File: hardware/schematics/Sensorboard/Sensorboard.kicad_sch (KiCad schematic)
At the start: 79 parts, among them J1 Grauwasser, J2 Switch/Solder Jumper, J3 BME680 #0 Innen, J5 BME280 #1 Außen, J6 HX711 GasWaage, J7 LT452 Malibu, J8 Frischwasser, J9 USB Power, Q1 IRLML2244, Q2 IRLML2244, Q3 IRLML2244, Q4 AO3401A, Q5 2N7002, Q6 IRLML2244, Q7 IRLML2244, U1 ESP32-S3-DevKitC, U2 TSR2-2450, U3 LDL1117S33R, U5 PCF8523T, U6 BNO055, U7 INA226, Y1 32.768, Y2 32.768

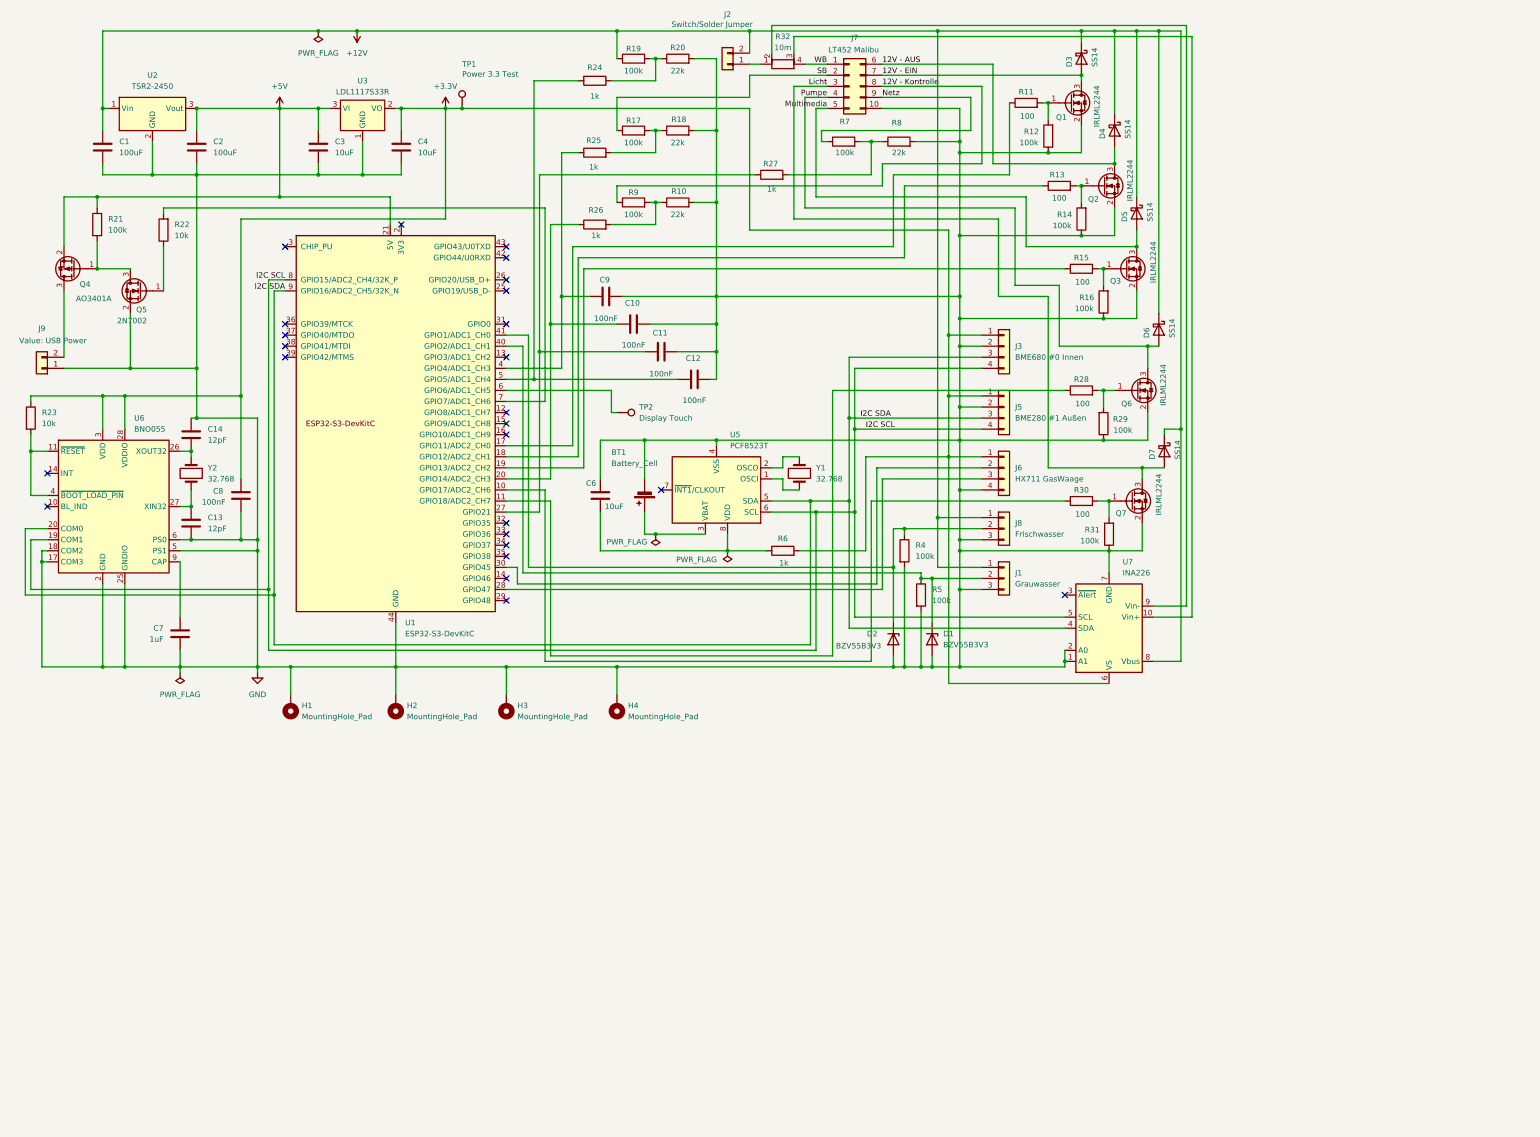
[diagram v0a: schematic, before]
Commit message: chore: OpenWiki, Sensorboard-/ruuvitag_gas-Schaltplaene, Log-Level und Doku nachgezogen
- OpenWiki-Index (openwiki/, AGENTS.md) und Verweis in CLAUDE.md
- Sensorboard-Schaltplan/PCB und ruuvitag_gas-Schaltplan aktualisiert
- LDL1117S33R-Bauteilbibliothek, Material-Icon-Font 16 px
- display_config.h: Log-Level Main/Theme auf WARN, Screenshot-Block aufgeraeumt
- gasbee_nrf/README: HX711-Modul und AVDD-Spannungsteiler beschrieben
- ruuvitag_hw (Fremd-Repo) in .gitignore

Co-Authored-By: Claude Opus 5.5 <noreply@anthropic.com>
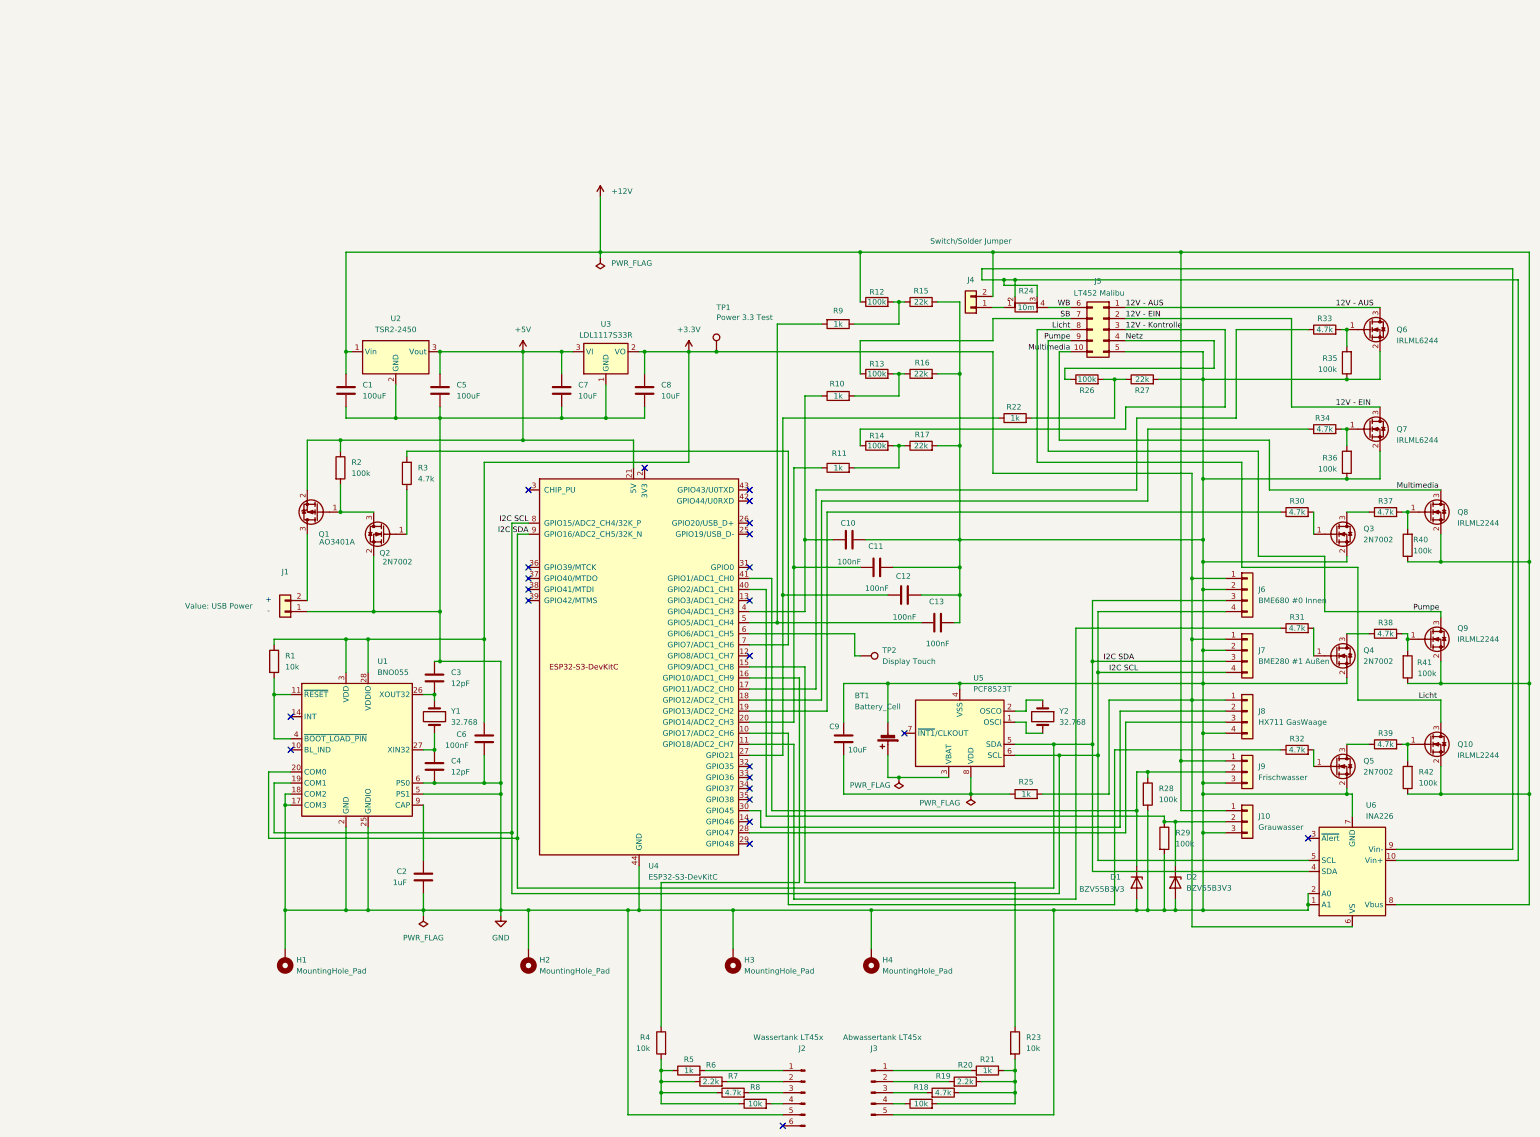
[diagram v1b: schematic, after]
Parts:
- removed D3, D4, D5, D6, D7: SS14, Diode_SMD:D_SMA, symbol Diode:SS14
- removed Q1, Q2: IRLML2244, Package_TO_SOT_SMD:SOT-23, symbol Transistor_FET:BSS138
- added J2: Wassertank LT45x, Connector_Molex:Molex_Micro-Fit_3.0_43650-0615_1x06_P3.00mm_Vertical, symbol Connector:Conn_01x06_Pin
- added J3: Abwassertank LT45x, Connector_Molex:Molex_Micro-Fit_3.0_43650-0515_1x05_P3.00mm_Vertical, symbol Connector:Conn_01x05_Pin
- added Q3, Q4, Q5: 2N7002, Package_TO_SOT_SMD:SOT-23, symbol Transistor_FET:2N7002
- added Q6, Q7: IRLML6244, Package_TO_SOT_SMD:SOT-23, symbol Transistor_FET:IRLML6244
- added R18, R23, R4, R8: 10k, Resistor_SMD:R_0402_1005Metric, symbol Device:R
- added R19, R30, R31, R32, R7: 4.7k, Resistor_SMD:R_0402_1005Metric, symbol Device:R
- added R20, R6: 2.2k, Resistor_SMD:R_0402_1005Metric, symbol Device:R
- added R21, R5: 1k, Resistor_SMD:R_0402_1005Metric, symbol Device:R
- R3: renamed from R22; value 10k -> 4.7k
- R33: renamed from R11; value 100 -> 4.7k
- R34: renamed from R13; value 100 -> 4.7k
- R37: renamed from R15; value 100 -> 4.7k
- R38: renamed from R28; value 100 -> 4.7k
- R39: renamed from R30; value 100 -> 4.7k
- renumbered C9 to C10, C10 to C11, C11 to C12, C12 to C13, C7 to C2, C14 to C3, C13 to C4, C2 to C5, C8 to C6, C3 to C7, C4 to C8, C6 to C9, D2 to D1, D1 to D2, J9 to J1, J1 to J10, J2 to J4, J7 to J5, J3 to J6, J5 to J7, J6 to J8, J8 to J9, Q4 to Q1, Q7 to Q10, Q5 to Q2, Q3 to Q8, Q6 to Q9, R23 to R1, R25 to R10, R26 to R11, R19 to R12, R17 to R13, R9 to R14, R20 to R15, R18 to R16, R10 to R17, R21 to R2, R27 to R22, R32 to R24, R6 to R25, R7 to R26, R8 to R27, R4 to R28, R5 to R29, R12 to R35, R14 to R36, R16 to R40, R29 to R41, R31 to R42, R24 to R9, U6 to U1, U1 to U4, U7 to U6, Y2 to Y1, Y1 to Y2
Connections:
- net +12V: now also Q10.2 (S), Q8.2 (S), Q9.2 (S), R40.1, R41.1, R42.1
- net 12V - AUS: now also J5.1 (Pin_1), Q6.3 (D); no longer J5.6 (Pin_6)
- net 12V - EIN: now also J5.2 (Pin_2), Q7.3 (D); no longer J5.7 (Pin_7)
- net 12V - Kontrolle: now also J5.3 (Pin_3); no longer J5.8 (Pin_8)
- net GND: now also J5.5 (Pin_5), J2.5 (Pin_5), J3.5 (Pin_5), Q3.2 (S), Q4.2 (S), Q5.2 (S), Q6.2 (S), Q7.2 (S); no longer J5.10 (Pin_10), Q10.2 (S), Q8.2 (S), Q9.2 (S), R40.1, R41.1, R42.1
- net Licht: now also J5.8 (Pin_8); no longer J5.3 (Pin_3)
- net Multimedia: now also J5.10 (Pin_10); no longer J5.5 (Pin_5)
- net Netz: now also J5.4 (Pin_4); no longer J5.9 (Pin_9)
- net Pumpe: now also J5.9 (Pin_9); no longer J5.4 (Pin_4)
- net SB: now also J5.7 (Pin_7); no longer J5.2 (Pin_2)
- net WB: now also J5.6 (Pin_6); no longer J5.1 (Pin_1)
- net at R38.1: now also Q4.3 (D); no longer U4.11 (GPIO18/ADC2_CH7)
- net at R34.2, R36.2: now also Q7.1 (G)
- net at R33.2, R35.2: now also Q6.1 (G)
- net at R24.2, U6.9 (Vin-): now also R24.3, U6.10 (Vin+)
- net at R39.1: now also Q5.3 (D); no longer U4.10 (GPIO17/ADC2_CH6)
- net at U4.15 (GPIO9/ADC1_CH8): now also R23.1
- net at U4.16 (GPIO10/ADC1_CH9): now also R4.1
- net at U4.19 (GPIO13/ADC2_CH2): now also R30.1; no longer R37.1
- new net: R18.2, R19.1, R20.1, R21.1, R23.2
- new net: J3.1 (Pin_1), R21.2
- new net: R4.2, R5.1, R6.1, R7.1, R8.1
- new net: J2.2 (Pin_2), R6.2
- new net: J3.3 (Pin_3), R19.2
- new net: Q3.1 (G), R30.2
- new net: Q3.3 (D), R37.1
- new net: J2.1 (Pin_1), R5.2
- new net: Q4.1 (G), R31.2
- new net: Q5.1 (G), R32.2
- new net: J2.4 (Pin_4), R8.2
- new net: R32.1, U4.10 (GPIO17/ADC2_CH6)
- new net: R31.1, U4.11 (GPIO18/ADC2_CH7)
- new net: J3.4 (Pin_4), R18.1
- new net: J2.3 (Pin_3), R7.2
- new net: J3.2 (Pin_2), R20.2
- no-connect marks 25 -> 24
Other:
- note added: "+"
- note added: "-"
- moved on the sheet: BT1, C1, C10, C11, C12, C13, C2, C3, C4, C5, C6, C7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
